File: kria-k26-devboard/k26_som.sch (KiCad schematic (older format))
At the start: 2 parts

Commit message: Finished adding signals to connector, create hierarchical schematic sheet structure
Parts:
- added M?: XILINX-KRIA-K26, antmicro-footprints:XILINX-KRIA-K26, symbol antmicroModules:XILINX-KRIA-K26
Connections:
- net GND: now also J_SOM240_1.C02, J_SOM240_1.C05, J_SOM240_1.C08, J_SOM240_1.C11, J_SOM240_1.C14, J_SOM240_1.C17, J_SOM240_2.A01, J_SOM240_2.A02, J_SOM240_2.A05, J_SOM240_2.A06, J_SOM240_2.A09, J_SOM240_2.A10, J_SOM240_2.A13, J_SOM240_2.A16, J_SOM240_2.A19, J_SOM240_2.A22, J_SOM240_2.A25, J_SOM240_2.A28, J_SOM240_2.A31, J_SOM240_2.A34, J_SOM240_2.A37, J_SOM240_2.A40, J_SOM240_2.A43, J_SOM240_2.A45, J_SOM240_2.A49, J_SOM240_2.A53, J_SOM240_2.A57, J_SOM240_2.B03, J_SOM240_2.B04, J_SOM240_2.B07, J_SOM240_2.B08, J_SOM240_2.B11, J_SOM240_2.B14, J_SOM240_2.B17, J_SOM240_2.B20, J_SOM240_2.B23, J_SOM240_2.B26, J_SOM240_2.B29, J_SOM240_2.B32, J_SOM240_2.B35, J_SOM240_2.B38, J_SOM240_2.B41, J_SOM240_2.B43, J_SOM240_2.B47, J_SOM240_2.B51, J_SOM240_2.B55, J_SOM240_2.C01, J_SOM240_2.C02, J_SOM240_2.C05, J_SOM240_2.C06, J_SOM240_2.C09, J_SOM240_2.C10, J_SOM240_2.C13, J_SOM240_2.C16, J_SOM240_2.C19, J_SOM240_2.C22, J_SOM240_2.C25, J_SOM240_2.C28, J_SOM240_2.C31, J_SOM240_2.C34, J_SOM240_2.C37, J_SOM240_2.C40, J_SOM240_2.C43, J_SOM240_2.C45, J_SOM240_2.C49, J_SOM240_2.C53, J_SOM240_2.C57, J_SOM240_2.D03, J_SOM240_2.D04, J_SOM240_2.D07, J_SOM240_2.D08, J_SOM240_2.D11, J_SOM240_2.D14, J_SOM240_2.D17, J_SOM240_2.D20, J_SOM240_2.D23, J_SOM240_2.D26, J_SOM240_2.D29, J_SOM240_2.D32, J_SOM240_2.D35, J_SOM240_2.D38, J_SOM240_2.D41, J_SOM240_2.D43, J_SOM240_2.D47, J_SOM240_2.D51, J_SOM240_2.D55
- net GTH_REFCLK0_C2M_P: now reaches J_SOM240_2.C03
- net GTH_REFCLK0_C2M_N: now reaches J_SOM240_2.C04
- net GTH_DP1_M2C_P: now reaches J_SOM240_2.C07
- net GTH_DP1_M2C_N: now reaches J_SOM240_2.C08
- net HPB09_P: now reaches J_SOM240_2.C11
- net HPB09_N: now reaches J_SOM240_2.C12
- net HPB14_P: now reaches J_SOM240_2.C14
- net HPB14_N: now reaches J_SOM240_2.C15
- net HPB02_P: now reaches J_SOM240_2.C17
- net HPB02_N: now reaches J_SOM240_2.C18
- net HPB13_P: now reaches J_SOM240_2.C20
- net HPB13_N: now reaches J_SOM240_2.C21
- net HPB_18_P: now reaches J_SOM240_2.C23
- net HPB_18_N: now reaches J_SOM240_2.C24
- net HPC17_P: now reaches J_SOM240_2.C26
- net HPC17_N: now reaches J_SOM240_2.C27
- net HPC10_CC_P: now reaches J_SOM240_2.C29
- net HPC10_CC_N: now reaches J_SOM240_2.C30
- net HPC11_P: now reaches J_SOM240_2.C32
- net HPC11_N: now reaches J_SOM240_2.C33
- net HPC12_P: now reaches J_SOM240_2.C35
- net HPC12_N: now reaches J_SOM240_2.C36
- net HPC05_CC_P: now reaches J_SOM240_2.C38
- net HPC05_CC_N: now reaches J_SOM240_2.C39
- net HPC_CLK0_P: now reaches J_SOM240_2.C41
- net HPC_CLK0_N: now reaches J_SOM240_2.C42
- net VCCO_HPC: now reaches J_SOM240_2.C44
- net VCCO_HPC: now also J_SOM240_2.D42
- net HDB06: now reaches J_SOM240_2.C46
- net HDB07: now reaches J_SOM240_2.C47
- net HDB08_CC: now reaches J_SOM240_2.C48
- net HDB09: now reaches J_SOM240_2.C50
- net HDB10: now reaches J_SOM240_2.C51
- net HDB11: now reaches J_SOM240_2.C52
- net HDC06: now reaches J_SOM240_2.C54
- net HDC07: now reaches J_SOM240_2.C55
- net HDC08_CC: now reaches J_SOM240_2.C56
- net HDC09: now reaches J_SOM240_2.C58
- net HDC10: now reaches J_SOM240_2.C59
- net HDC11: now reaches J_SOM240_2.C60
- net GTH_DP1_C2M_P: now reaches J_SOM240_2.D01
- net GTH_DP1_C2M_N: now reaches J_SOM240_2.D02
- net GTH_DP3_C2M_P: now reaches J_SOM240_2.D05
- net GTH_DP3_C2M_N: now reaches J_SOM240_2.D06
- net GTH_DP0_M2C_P: now reaches J_SOM240_2.D09
- net GTH_DP0_M2C_N: now reaches J_SOM240_2.D10
- net HPB01_P: now reaches J_SOM240_2.D12
- net HPB01_N: now reaches J_SOM240_2.D13
- net HPB00_CC_P: now reaches J_SOM240_2.D15
- net HPB00_CC_N: now reaches J_SOM240_2.D16
- net HPB_CLK0_P: now reaches J_SOM240_2.D18
- net HPB_CLK0_N: now reaches J_SOM240_2.D19
- net HPB04_P: now reaches J_SOM240_2.D21
- net HPB04_N: now reaches J_SOM240_2.D22
- net HPB17_P: now reaches J_SOM240_2.D24
- net HPB17_N: now reaches J_SOM240_2.D25
- net HPC09_P: now reaches J_SOM240_2.D27
- net HPC09_N: now reaches J_SOM240_2.D28
- net HPC01_P: now reaches J_SOM240_2.D30
- net HPC01_N: now reaches J_SOM240_2.D31
- net HPC00_CC_P: now reaches J_SOM240_2.D33
- net HPC00_CC_N: now reaches J_SOM240_2.D34
- net HPC02_P: now reaches J_SOM240_2.D36
- net HPC02_N: now reaches J_SOM240_2.D37
- net HPC04_P: now reaches J_SOM240_2.D39
- net HPC04_N: now reaches J_SOM240_2.D40
- net HDB00_CC: now reaches J_SOM240_2.D44
- net HDB01: now reaches J_SOM240_2.D45
- net HDB02: now reaches J_SOM240_2.D46
- net HDB03: now reaches J_SOM240_2.D48
- net HDB04: now reaches J_SOM240_2.D49
- net HDB05: now reaches J_SOM240_2.D50
- net HDC00_CC: now reaches J_SOM240_2.D52
- net HDC01: now reaches J_SOM240_2.D53
- net HDC02: now reaches J_SOM240_2.D54
- net HDC03: now reaches J_SOM240_2.D56
- net HDC04: now reaches J_SOM240_2.D57
- net HDC05: now reaches J_SOM240_2.D58
- net VCCO_HDC: now reaches J_SOM240_2.D59
- net VCCO_HDC: now also J_SOM240_2.D60
- net GTH_DP3_M2C_P: now reaches J_SOM240_2.A03
- net GTH_DP3_M2C_N: now reaches J_SOM240_2.A04
- net GTH_REFCLK1_C2M_P: now reaches J_SOM240_2.A07
- net GTH_REFCLK1_C2M_N: now reaches J_SOM240_2.A08
- net HPB15_CC_P: now reaches J_SOM240_2.A11
- net HPB_15_CC_N: now reaches J_SOM240_2.A12
- net HPB08_P: now reaches J_SOM240_2.A14
- net HPB08_N: now reaches J_SOM240_2.A15
- net HPB12_P: now reaches J_SOM240_2.A17
- net HPB12_N: now reaches J_SOM240_2.A18
- net HPB06_P: now reaches J_SOM240_2.A20
- net HPB06_N: now reaches J_SOM240_2.A21
- net HPB16_P: now reaches J_SOM240_2.A23
- net HPB16_N: now reaches J_SOM240_2.A24
- net HPB19_P: now reaches J_SOM240_2.A26
- net HPB19_N: now reaches J_SOM240_2.A27
- net HPC08_P: now reaches J_SOM240_2.A29
- net HPC08_N: now reaches J_SOM240_2.A30
- net HPC19_P: now reaches J_SOM240_2.A32
- net HPC19_N: now reaches J_SOM240_2.A33
- net HPC14_P: now reaches J_SOM240_2.A35
- net HPC14_N: now reaches J_SOM240_2.A36
- net HPC15_CC_P: now reaches J_SOM240_2.A38
- net HPC15_CC_N: now reaches J_SOM240_2.A39
- net HPC03_P: now reaches J_SOM240_2.A41
- net HPC03_N: now reaches J_SOM240_2.A42
- net VCCO_HPB: now reaches J_SOM240_2.A44
- net VCCO_HPB: now also J_SOM240_2.B42
- net HDB18: now reaches J_SOM240_2.A46
- net HDB19: now reaches J_SOM240_2.A47
- net HDB20: now reaches J_SOM240_2.A48
- net HDB21: now reaches J_SOM240_2.A50
- net HDB22: now reaches J_SOM240_2.A51
- net HDB23: now reaches J_SOM240_2.A52
- net HDC18: now reaches J_SOM240_2.A54
- net HDC19: now reaches J_SOM240_2.A55
- net HDC20: now reaches J_SOM240_2.A56
- net HDC21: now reaches J_SOM240_2.A58
- net HDC22: now reaches J_SOM240_2.A59
- net HDC23: now reaches J_SOM240_2.A60
- net GTH_DP2_C2M_P: now reaches J_SOM240_2.B01
- net GTH_DP2_C2M_N: now reaches J_SOM240_2.B02
- net GTH_DP2_M2C_P: now reaches J_SOM240_2.B05
- net GTH_DP2_M2C_N: now reaches J_SOM240_2.B06
- net GTH_DP0_C2M_P: now reaches J_SOM240_2.B09
- net GTH_DP0_C2M_N: now reaches J_SOM240_2.B10
- net HPB10_CC_P: now reaches J_SOM240_2.B12
- net HPB10_CC_N: now reaches J_SOM240_2.B13
- net HPB07_P: now reaches J_SOM240_2.B15
- net HPB07_N: now reaches J_SOM240_2.B16
- net HPB05_CC_P: now reaches J_SOM240_2.B18
- net HPB05_CC_N: now reaches J_SOM240_2.B19
- net HPB11_P: now reaches J_SOM240_2.B21
- net HPB11_N: now reaches J_SOM240_2.B22
- net HPB03_P: now reaches J_SOM240_2.B24
- net HPB03_N: now reaches J_SOM240_2.B25
- net HPC06_P: now reaches J_SOM240_2.B27
- net HPC06_N: now reaches J_SOM240_2.B28
- net HPC13_P: now reaches J_SOM240_2.B30
- net HPC13_N: now reaches J_SOM240_2.B31
- net HPC16_P: now reaches J_SOM240_2.B33
- net HPC16_N: now reaches J_SOM240_2.B34
- net HPC07_P: now reaches J_SOM240_2.B36
- net HPC07_N: now reaches J_SOM240_2.B37
- net HPC18_P: now reaches J_SOM240_2.B39
- net HPC18_N: now reaches J_SOM240_2.B40
- net HDB12: now reaches J_SOM240_2.B44
- net HDB13: now reaches J_SOM240_2.B45
- net HDB14: now reaches J_SOM240_2.B46
- net HDB15: now reaches J_SOM240_2.B48
- net HDB16_CC: now reaches J_SOM240_2.B49
- net HDB17: now reaches J_SOM240_2.B50
- net HDC12: now reaches J_SOM240_2.B52
- net HDC13: now reaches J_SOM240_2.B53
- net HDC14: now reaches J_SOM240_2.B54
- net HDC15: now reaches J_SOM240_2.B56
- net HDC16_CC: now reaches J_SOM240_2.B57
- net HDC17: now reaches J_SOM240_2.B58
- net VCCO_HDB: now reaches J_SOM240_2.B59
- net VCCO_HDB: now also J_SOM240_2.B60
- net HPA00_CC_P: now reaches J_SOM240_1.C03
- net HPA00_CC_N: now reaches J_SOM240_1.C04
- net HPA03_P: now reaches J_SOM240_1.C06
- net HPA03_N: now reaches J_SOM240_1.C07
- net HPA08_P: now reaches J_SOM240_1.C09
- net HPA08_N: now reaches J_SOM240_1.C10
- net HPA10_CC_P: now reaches J_SOM240_1.C12
- net HPA10_CC_N: now reaches J_SOM240_1.C13
- net PS_POR_L: now reaches J_SOM240_1.C15
- net PS_SRST_C2M_L: now reaches J_SOM240_1.C16
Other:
- moved on the sheet: J_SOM240_1B, J_SOM240_2A, J_SOM240_2B

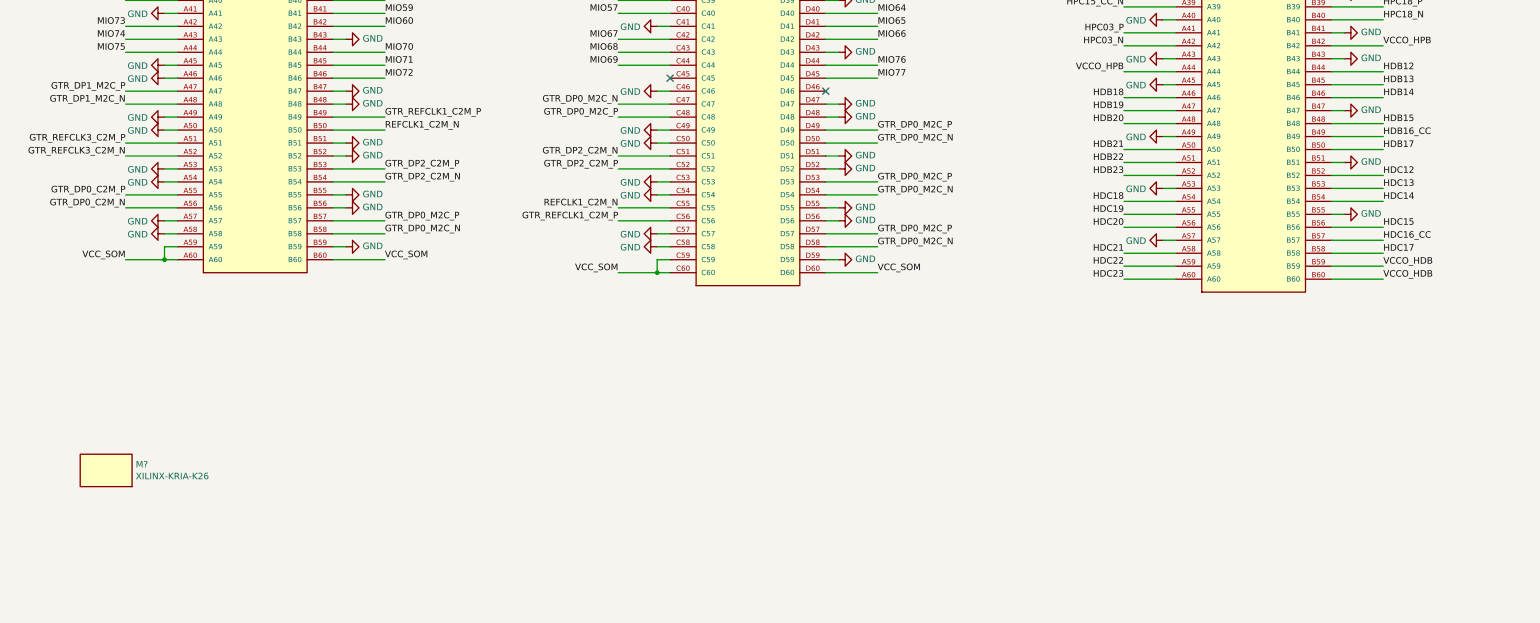
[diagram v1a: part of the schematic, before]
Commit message: First sketches of POE part of supply
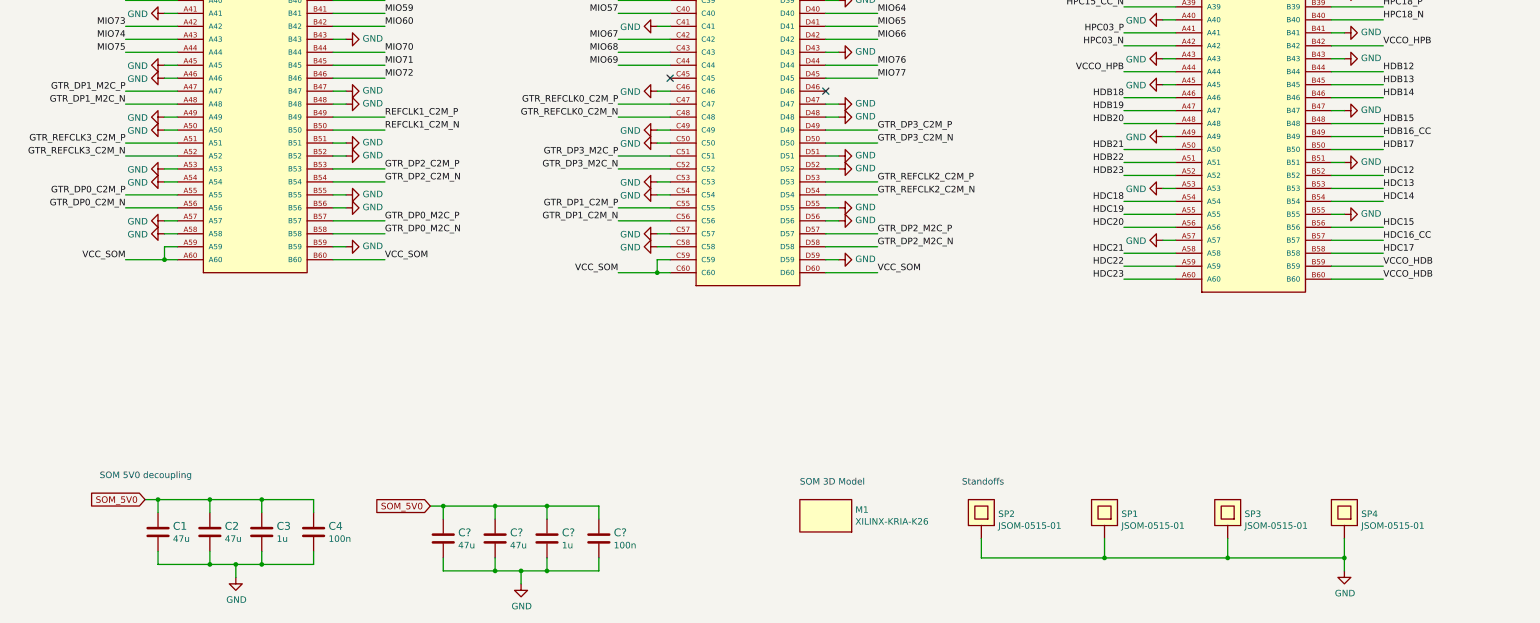
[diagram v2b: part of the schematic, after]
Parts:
- added C1, C2, C? (x2): C_47u_0805, antmicro-footprints:0805-cap, symbol antmicroCapacitorsmisc:C_47u_0805
- added C3, C?: C_1u_0402, antmicro-footprints:0402-cap, symbol antmicroCapacitors0402:C_1u_0402
- added C4, C?: C_100n_0402, antmicro-footprints:0402-cap, symbol antmicroCapacitors0402:C_100n_0402
- added SP1, SP2, SP3, SP4: JSOM-0515-01, antmicro-footprints:SAMTEC_JSOM-0515-01, symbol antmicroMechanicalParts:JSOM-0515-01
- gave numbers to parts that had none: 1
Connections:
- net GND: now also C1.2, C2.2, C3.2, C4.2, C?.2, C?.2, C?.2, C?.2, SP1.1, SP2.1, SP3.1, SP4.1
- net GTR_DP0_M2C_N: no longer J_SOM240_1.C47, J_SOM240_1.D50, J_SOM240_1.D54, J_SOM240_1.D58
- net GTR_DP0_M2C_P: no longer J_SOM240_1.C48, J_SOM240_1.D49, J_SOM240_1.D53, J_SOM240_1.D57
- net GTR_DP2_C2M_N: no longer J_SOM240_1.C51
- net GTR_DP2_C2M_P: no longer J_SOM240_1.C52
- net REFCLK1_C2M_N: no longer J_SOM240_1.C55
- net GTR_REFCLK1_C2M_P renamed GTR_DP1_C2M_N
- net GTR_DP1_C2M_N: no longer J_SOM240_1.B49
- new net GTR_DP1_C2M_P: J_SOM240_1.C55
- new net GTR_DP2_M2C_N: J_SOM240_1.D58
- new net GTR_DP2_M2C_P: J_SOM240_1.D57
- new net GTR_DP3_C2M_N: J_SOM240_1.D50
- new net GTR_DP3_C2M_P: J_SOM240_1.D49
- new net GTR_DP3_M2C_N: J_SOM240_1.C52
- new net GTR_DP3_M2C_P: J_SOM240_1.C51
- new net GTR_REFCLK0_C2M_N: J_SOM240_1.C48
- new net GTR_REFCLK0_C2M_P: J_SOM240_1.C47
- new net GTR_REFCLK2_C2M_N: J_SOM240_1.D54
- new net GTR_REFCLK2_C2M_P: J_SOM240_1.D53
- new net REFCLK1_C2M_P: J_SOM240_1.B49
- new net SOM_5V0: C1.1, C2.1, C3.1, C4.1, C?.1, C?.1, C?.1, C?.1
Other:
- note added: "SOM 3D Model"
- note added: "SOM 5V0 decoupling"
- note added: "Standoffs"
- moved on the sheet: M1

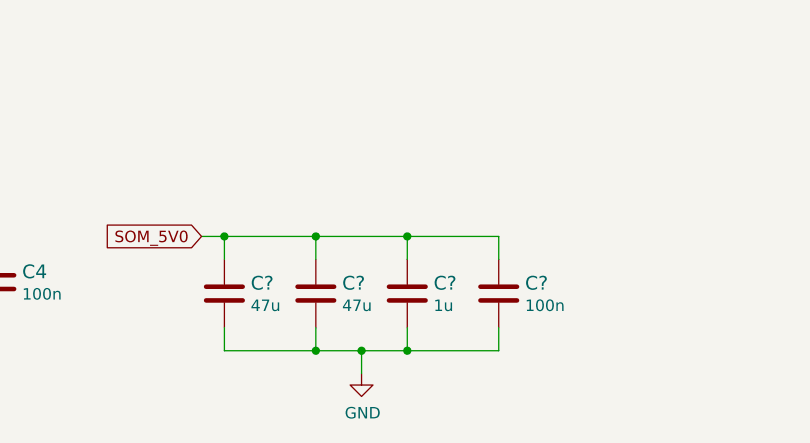
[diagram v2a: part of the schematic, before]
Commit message: Finished PoE part and DC-DC for PS and PL domains
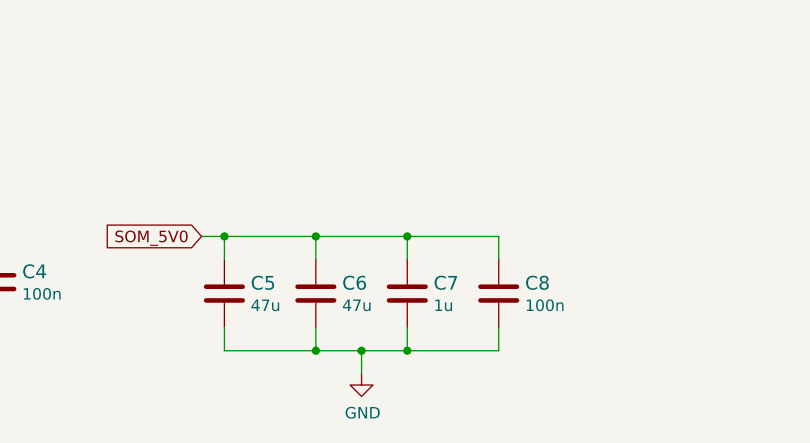
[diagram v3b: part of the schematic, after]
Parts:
- gave numbers to parts that had none: 4
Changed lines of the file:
@@
 $Descr A3 16535 11693
 encoding utf-8
-Sheet 2 7
+Sheet 2 9
 Title "K26 SOM connnector"
 Date ""
@@
 SOM 3D Model
 $Comp
-L antmicroCapacitorsmisc:C_47u_0805 C?
+L antmicroCapacitorsmisc:C_47u_0805 C5
 U 1 1 6235AEE5
 P 3850 10550
-F 0 "C?" H 3965 10595 60  0000 L CNN
+F 0 "C5" H 3965 10595 60  0000 L CNN
 F 1 "C_47u_0805" H 3850 10400 60  0001 C CNN
 F 2 "antmicro-footprints:0805-cap" H 4050 10750 60  0001 L CNN
@@
 $EndComp
 $Comp
-L antmicroCapacitorsmisc:C_47u_0805 C?
+L antmicroCapacitorsmisc:C_47u_0805 C6
 U 1 1 6235AEEE
 P 4250 10550
-F 0 "C?" H 4365 10595 60  0000 L CNN
+F 0 "C6" H 4365 10595 60  0000 L CNN
 F 1 "C_47u_0805" H 4250 10400 60  0001 C CNN
 F 2 "antmicro-footprints:0805-cap" H 4450 10750 60  0001 L CNN
@@
 $EndComp
 $Comp
-L antmicroCapacitors0402:C_1u_0402 C?
+L antmicroCapacitors0402:C_1u_0402 C7
 U 1 1 6235AEF7
 P 4650 10550
-F 0 "C?" H 4765 10595 60  0000 L CNN
+F 0 "C7" H 4765 10595 60  0000 L CNN
 F 1 "C_1u_0402" H 4650 10400 60  0001 C CNN
 F 2 "antmicro-footprints:0402-cap" H 4850 10750 60  0001 L CNN
@@
 $EndComp
 $Comp
-L antmicroCapacitors0402:C_100n_0402 C?
+L antmicroCapacitors0402:C_100n_0402 C8
 U 1 1 6235AF00
 P 5050 10550
-F 0 "C?" H 5165 10595 60  0000 L CNN
+F 0 "C8" H 5165 10595 60  0000 L CNN
 F 1 "C_100n_0402" H 5050 10400 60  0001 C CNN
 F 2 "antmicro-footprints:0402-cap" H 5250 10750 60  0001 L CNN
@@
 Connection ~ 3850 10300
 $Comp
-L power:GND #PWR?
+L power:GND #PWR0101
 U 1 1 6235AF1B
 P 4450 10900
-F 0 "#PWR?" H 4450 10650 50  0001 C CNN
+F 0 "#PWR0101" H 4450 10650 50  0001 C CNN
 F 1 "GND" H 4455 10727 50  0000 C CNN
 F 2 "" H 4450 10900 50  0001 C CNN

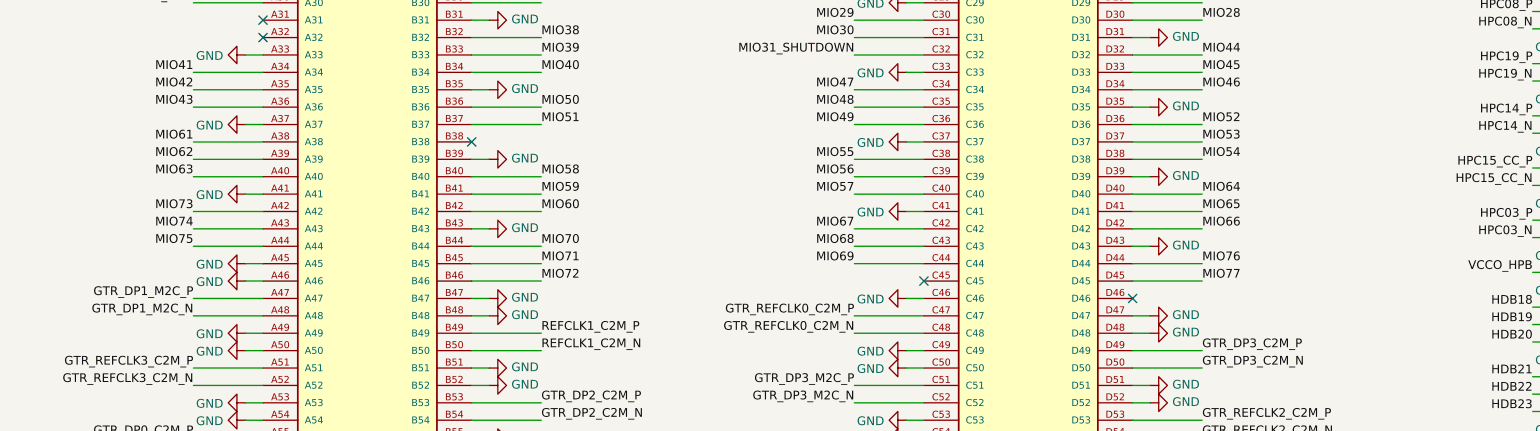
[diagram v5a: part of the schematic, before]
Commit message: Fixed VSS connection for OSC and LED pin in PoE POS section, first update of ETH schematic
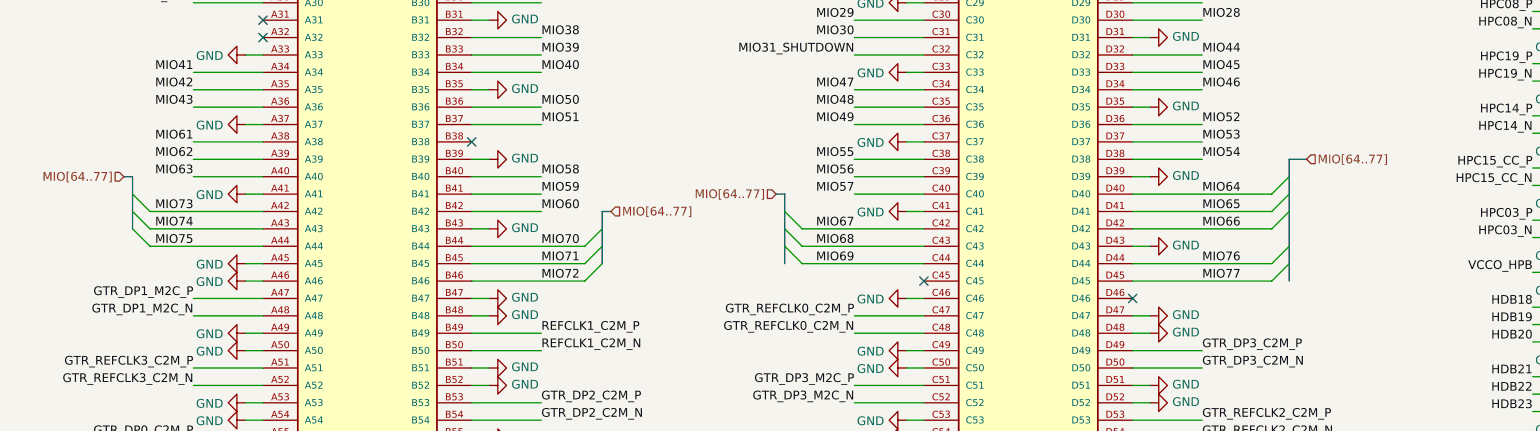
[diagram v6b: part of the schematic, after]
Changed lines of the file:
@@
 Text Label 1400 6700 2    50   ~ 0
 MIO74
-Wire Wire Line
-	1800 6700 1400 6700
-Text Label 1400 6600 2    50   ~ 0
-MIO73
-Wire Wire Line
-	1800 6600 1400 6600
 Text Label 1400 6800 2    50   ~ 0
 MIO75
 Wire Wire Line
-	1800 6800 1400 6800
-Wire Wire Line
 	1800 6900 1700 6900
 Wire Wire Line
@@
 	0    -1   -1   0
 $EndComp
-Wire Wire Line
-	3000 6800 3400 6800
 Text Label 3400 6800 0    50   ~ 0
 MIO70
-Wire Wire Line
-	3000 7000 3400 7000
 Text Label 3400 7000 0    50   ~ 0
 MIO72
-Wire Wire Line
-	3000 6900 3400 6900
 Text Label 3400 6900 0    50   ~ 0
 MIO71
@@
 Wire Wire Line
 	5500 6600 5600 6600
-Wire Wire Line
-	5600 6900 5200 6900
 Text Label 5200 6900 2    50   ~ 0
 MIO69
-Wire Wire Line
-	5600 6700 5200 6700
 Text Label 5200 6700 2    50   ~ 0
 MIO67
-Wire Wire Line
-	5600 6800 5200 6800
 Text Label 5200 6800 2    50   ~ 0
 MIO68
@@
 MIO65
 Wire Wire Line
-	6800 6500 7200 6500
-Wire Wire Line
-	7200 6600 6800 6600
-Wire Wire Line
 	6800 6400 6900 6400
 Text Label 7200 6700 0    50   ~ 0
 MIO66
-Wire Wire Line
-	7200 6700 6800 6700
 $Comp
 L power:GND #PWR0175
@@
 MIO77
 Wire Wire Line
-	6800 6900 7200 6900
-Wire Wire Line
-	7200 7000 6800 7000
-Wire Wire Line
 	6800 6800 6900 6800
 NoConn ~ 6800 7100
@@
 Text Notes 1200 10100 0    50   ~ 0
 SOM 5V0 decoupling
+Text HLabel 7800 6300 2    50   Input ~ 0
+MIO[64..77]
+Wire Bus Line
+	7800 6300 7700 6300
+Entry Wire Line
+	7600 6500 7700 6400
+Wire Wire Line
+	6800 6500 7600 6500
+Wire Wire Line
+	6800 6600 7600 6600
+Wire Wire Line
+	6800 6700 7600 6700
+Wire Wire Line
+	6800 6900 7600 6900
+Wire Wire Line
+	6800 7000 7600 7000
+Entry Wire Line
+	7600 6900 7700 6800
+Entry Wire Line
+	7600 7000 7700 6900
+Entry Wire Line
+	7600 6700 7700 6600
+Entry Wire Line
+	7600 6600 7700 6500
+Text HLabel 3800 6600 2    50   Input ~ 0
+MIO[64..77]
+Wire Bus Line
+	4750 6500 4800 6500
+Entry Wire Line
+	4900 6700 4800 6600
+Entry Wire Line
+	4900 6900 4800 6800
+Entry Wire Line
+	4900 6800 4800 6700
+Wire Wire Line
+	4900 6700 5600 6700
+Wire Wire Line
+	4900 6800 5600 6800
+Wire Wire Line
+	4900 6900 5600 6900
+Wire Wire Line
+	3000 6800 3650 6800
+Wire Wire Line
+	3000 6900 3650 6900
+Wire Wire Line
+	3000 7000 3650 7000
+Entry Wire Line
+	3650 6800 3750 6700
+Entry Wire Line
+	3650 6900 3750 6800
+Entry Wire Line
+	3650 7000 3750 6900
+Wire Wire Line
+	1150 6600 1800 6600
+Wire Wire Line
+	1150 6700 1800 6700
+Wire Wire Line
+	1150 6800 1800 6800
+Text HLabel 1000 6400 0    50   Input ~ 0
+MIO[64..77]
+Wire Bus Line
+	1000 6400 1050 6400
+Entry Wire Line
+	1150 6600 1050 6500
+Entry Wire Line
+	1150 6700 1050 6600
+Entry Wire Line
+	1150 6800 1050 6700
+Text Label 1400 6600 2    50   ~ 0
+MIO73
+Wire Bus Line
+	3750 6600 3800 6600
+Text HLabel 4750 6500 0    50   Input ~ 0
+MIO[64..77]
+Wire Bus Line
+	3750 6600 3750 6900
+Wire Bus Line
+	1050 6400 1050 6700
+Wire Bus Line
+	4800 6500 4800 6900
+Wire Bus Line
+	7700 6300 7700 7000
 $EndSCHEMATC

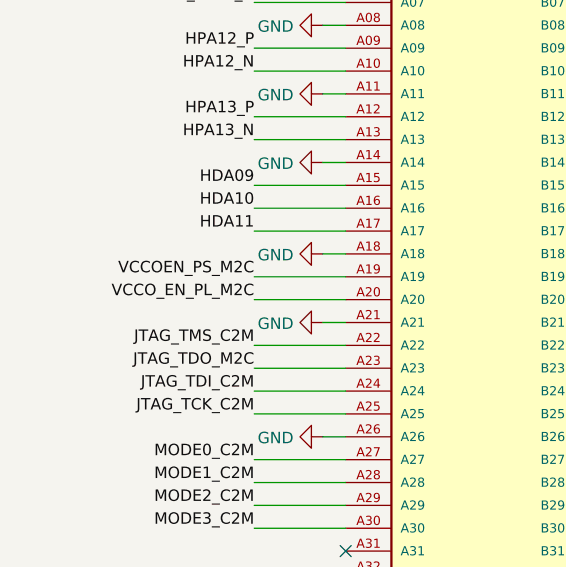
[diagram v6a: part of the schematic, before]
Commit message: Finished ETH part of the schematic
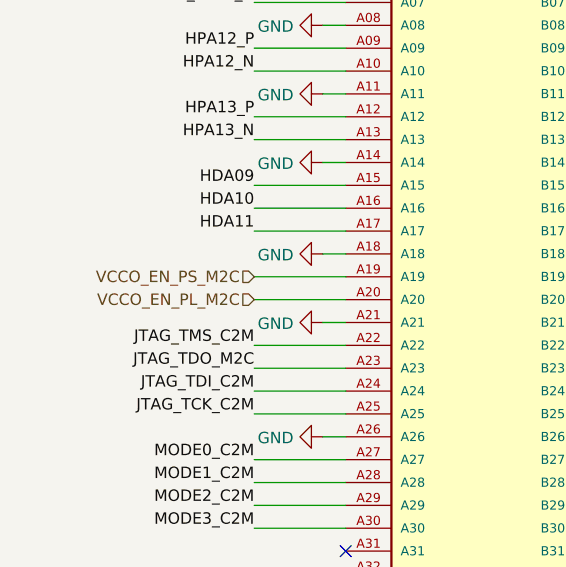
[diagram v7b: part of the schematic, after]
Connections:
- net VCCOEN_PS_M2C renamed VCCO_EN_PS_M2C
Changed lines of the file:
@@
 Wire Wire Line
 	1800 4200 1700 4200
-Text Label 1400 4400 2    50   ~ 0
-VCCO_EN_PL_M2C
 Wire Wire Line
 	1800 4400 1400 4400
-Text Label 1400 4300 2    50   ~ 0
-VCCOEN_PS_M2C
 Wire Wire Line
 	1800 4300 1400 4300
@@
 Wire Bus Line
 	7700 6300 7700 7000
+Text HLabel 1400 4400 0    50   Input ~ 0
+VCCO_EN_PL_M2C
+Text HLabel 1400 4300 0    50   Input ~ 0
+VCCO_EN_PS_M2C
 $EndSCHEMATC
